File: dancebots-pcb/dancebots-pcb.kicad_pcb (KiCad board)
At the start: 2 copper layers, 50 x 50 mm, 33 parts, among them J1 BATTERY, J2 MOT2-L, J3 MOT1-R, J4 MP3 Player, U1 L4941, U2 L293, U3 ATTINY861A-P, U4 LM386, U5 LM358

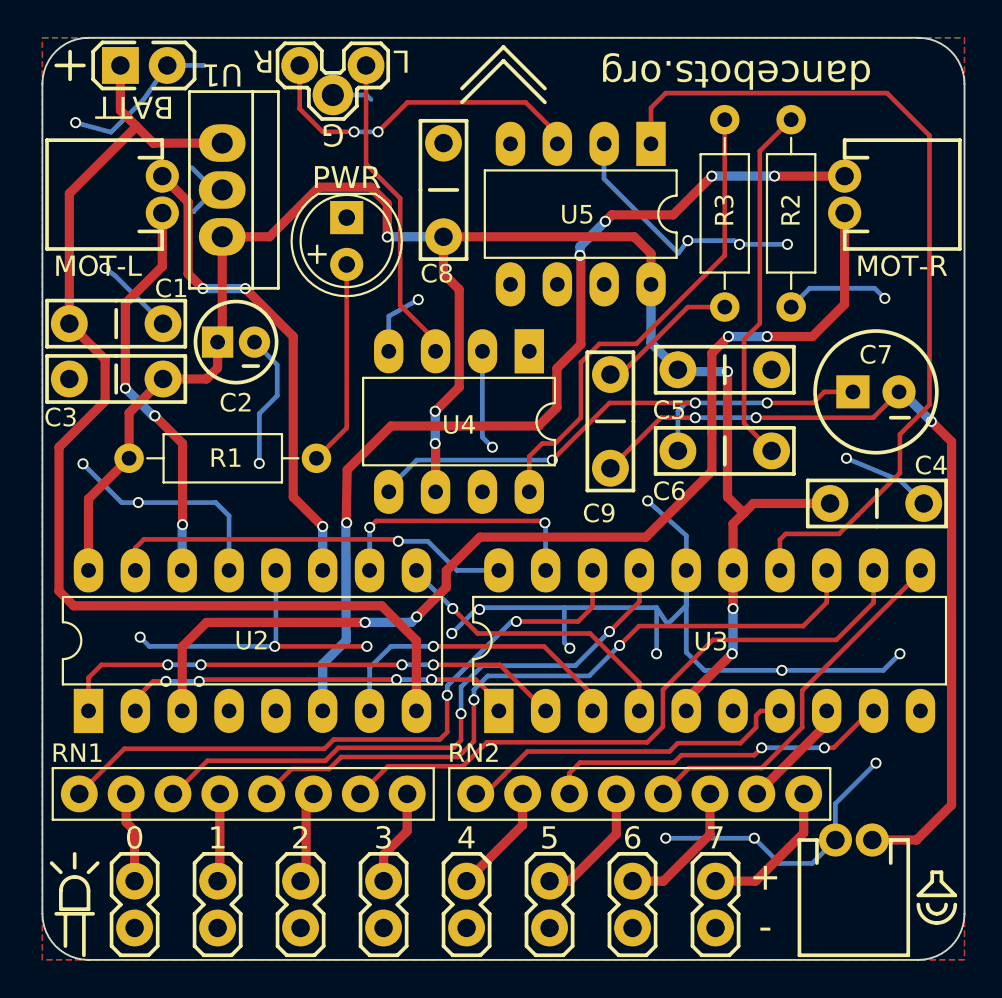
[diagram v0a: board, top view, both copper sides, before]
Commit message: changed fp slightly after first iteration
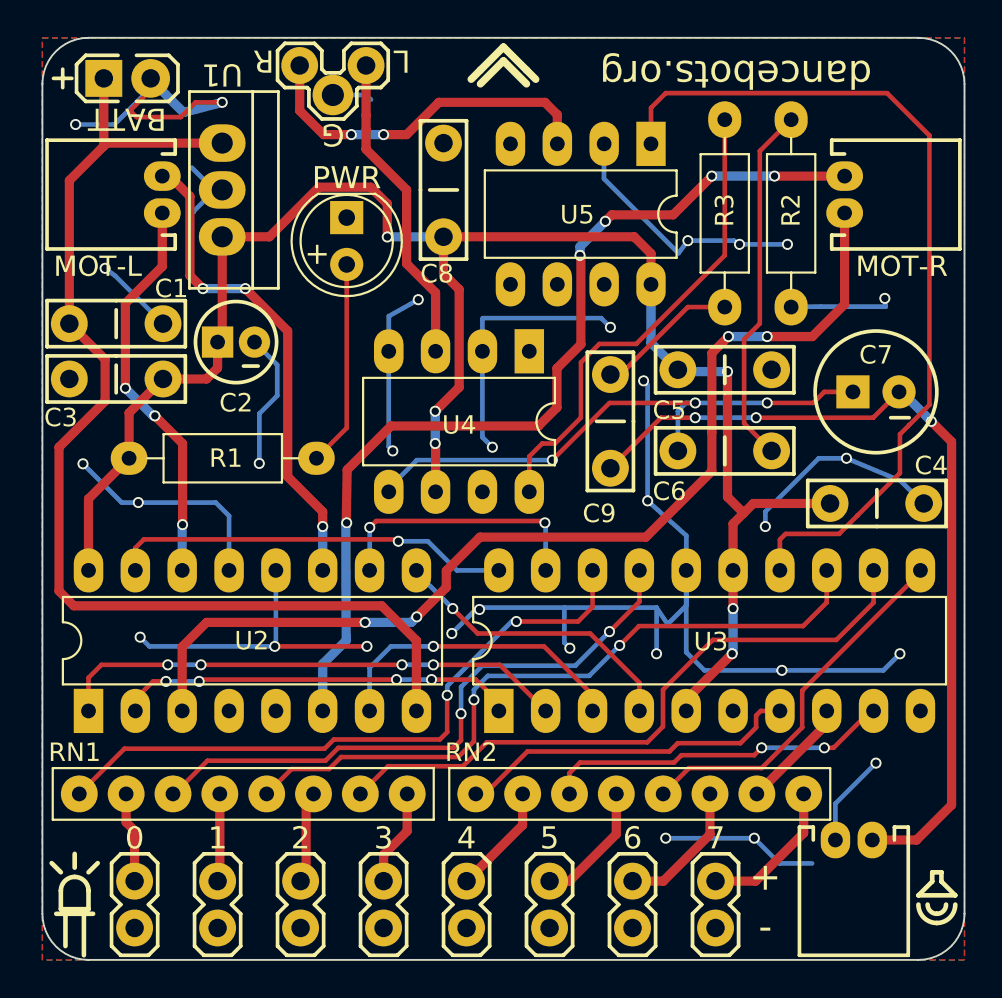
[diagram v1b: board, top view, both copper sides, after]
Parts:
- moved J1 1.14 mm to (104.6, 102.2)
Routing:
- net GND: track 147.7 -> 182.3 mm, vias 25 -> 30
- net /MP3_R: track 18.7 -> 20.1 mm
- net /MP3_L: track 17.1 -> 17.7 mm

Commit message: shrunk CAP holes to 0.8mm
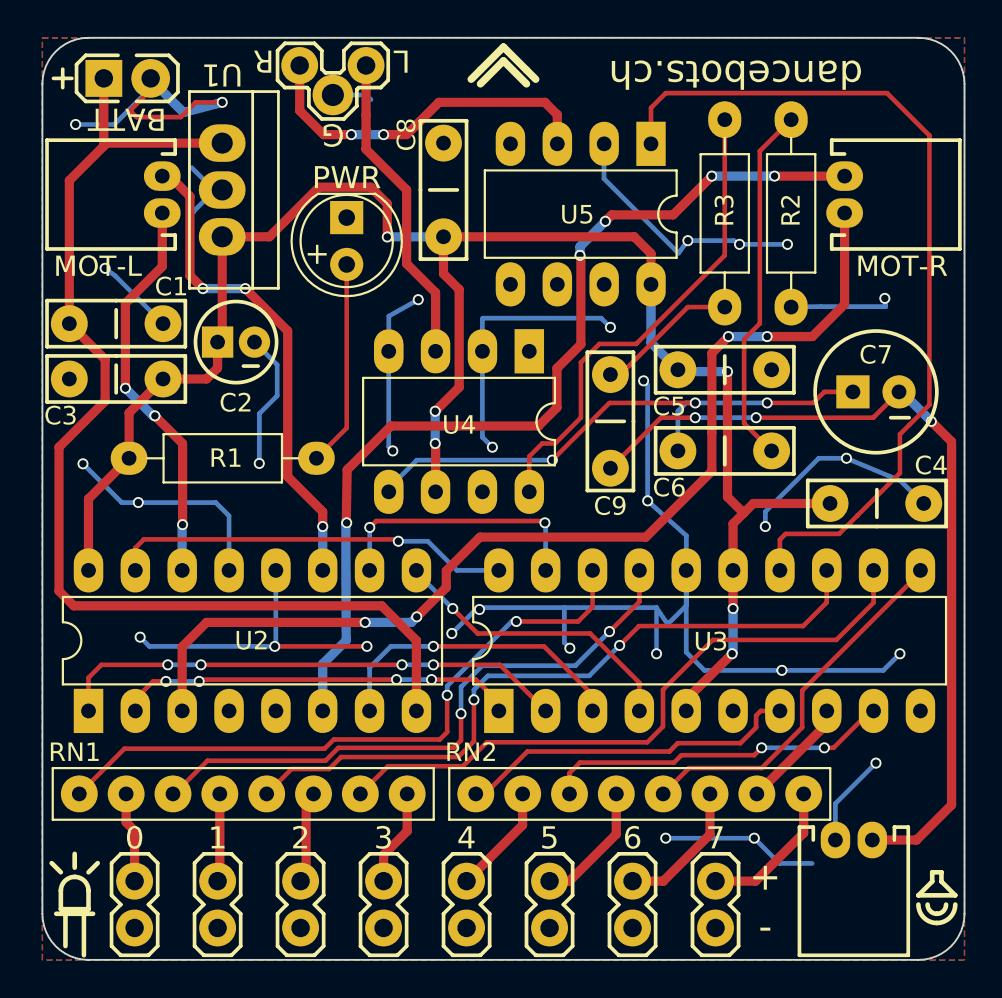
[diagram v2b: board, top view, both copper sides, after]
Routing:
- net (no net): track 0.00 -> 8.85 mm, vias 0 -> 2
- net GND: track 182.3 -> 173.4 mm, vias 30 -> 28
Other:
- board text added: "dancebots.ch"
- board text removed: "dancebots.org"
